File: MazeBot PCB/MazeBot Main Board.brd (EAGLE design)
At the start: 160 x 100 mm, 42 parts, among them IC1 7805TV, IC2 L298, U1 38kHz

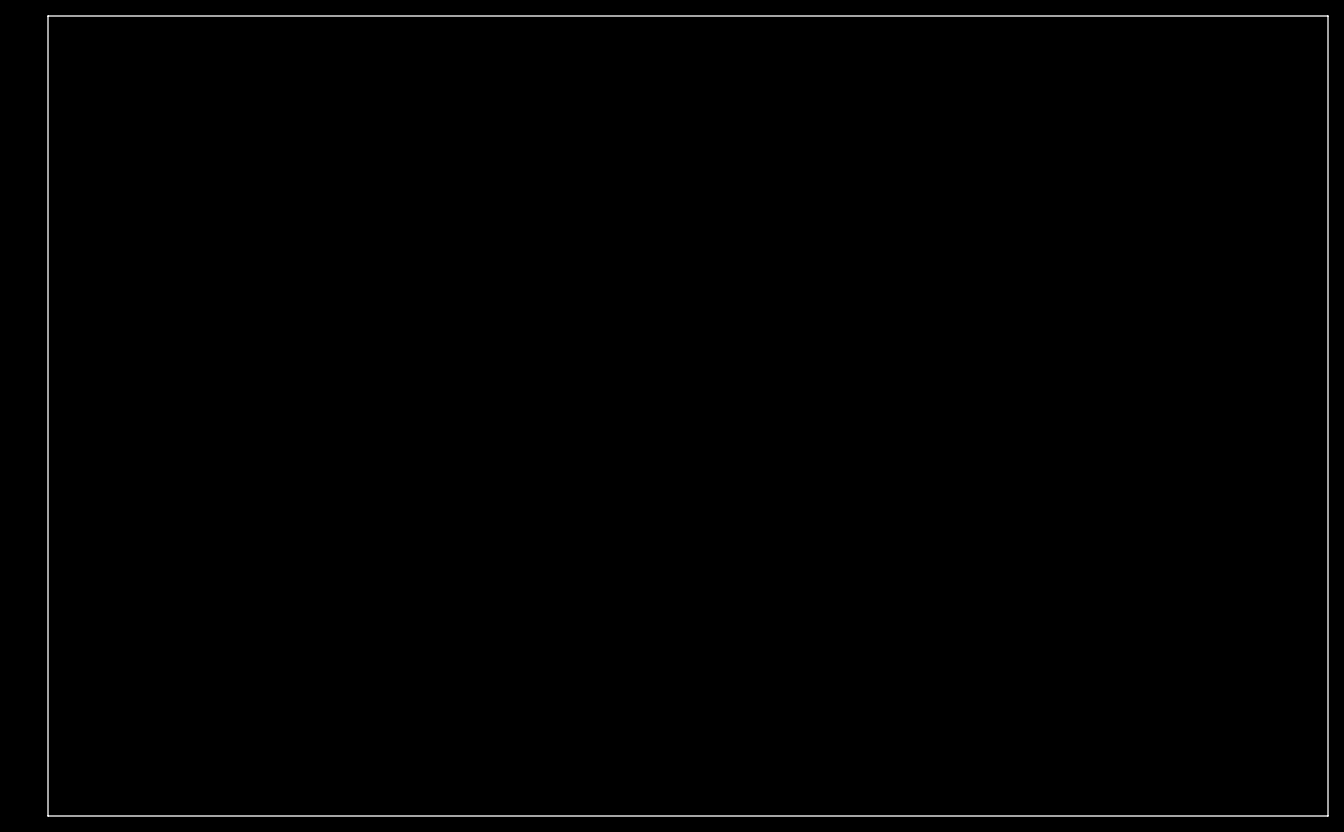
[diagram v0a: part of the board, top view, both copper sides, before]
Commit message: Fix minor shematic issues
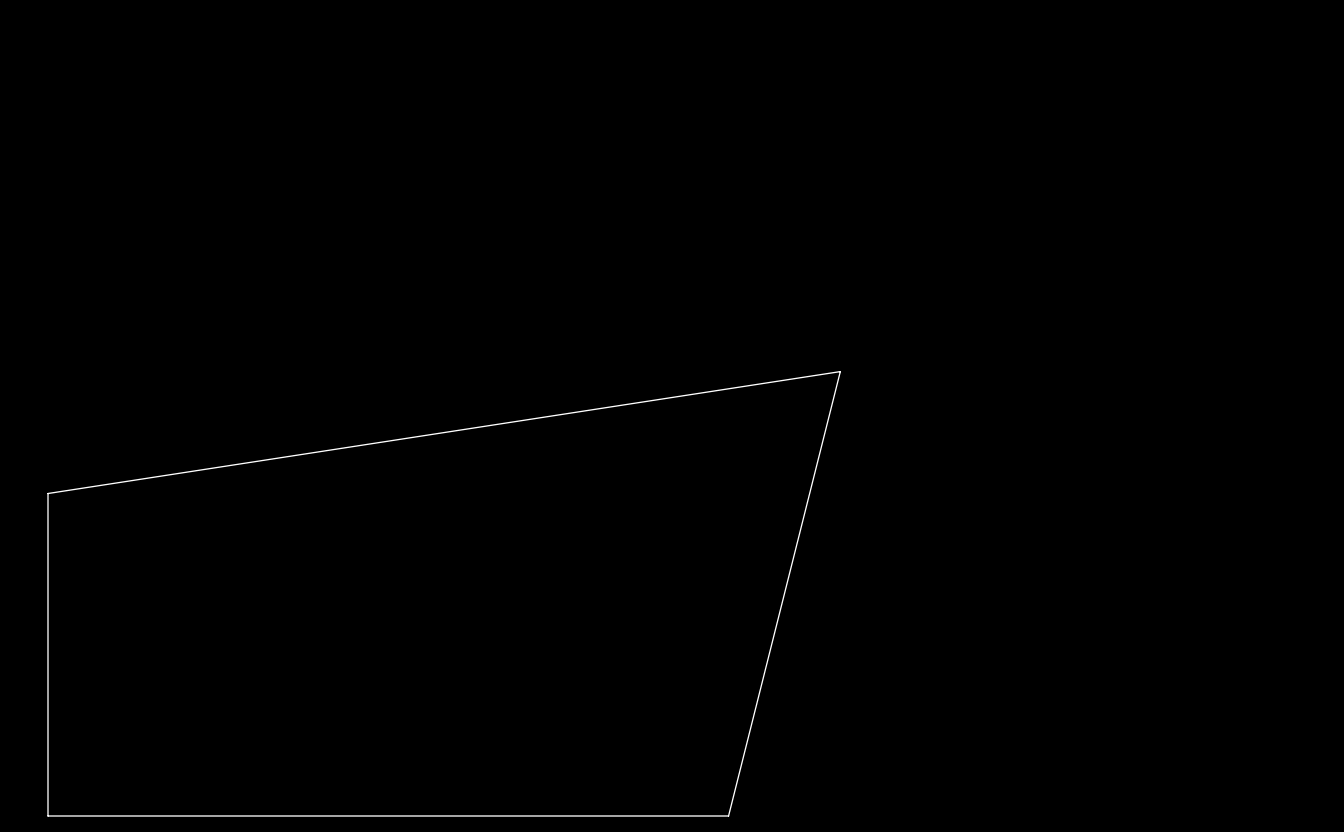
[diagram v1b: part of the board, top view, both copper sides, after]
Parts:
- Q1: value (none) -> 16MHz
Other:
- board size 160 x 100 mm -> 99 x 55.5 mm
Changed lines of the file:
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@@
 <board>
 <plain>
-<wire x1="0" y1="0" x2="160" y2="0" width="0" layer="20"/>
-<wire x1="160" y1="0" x2="160" y2="100" width="0" layer="20"/>
-<wire x1="160" y1="100" x2="0" y2="100" width="0" layer="20"/>
-<wire x1="0" y1="100" x2="0" y2="0" width="0" layer="20"/>
+<wire x1="0" y1="0" x2="85.07" y2="0" width="0" layer="20"/>
+<wire x1="85.07" y1="0" x2="99.04" y2="55.55" width="0" layer="20"/>
+<wire x1="99.04" y1="55.55" x2="0" y2="40.31" width="0" layer="20"/>
+<wire x1="0" y1="40.31" x2="0" y2="0" width="0" layer="20"/>
+<dimension x1="0" y1="100" x2="128.27" y2="100.33" x3="64.08593125" y3="119.237746875" textsize="1.778" layer="1"/>
 </plain>
 <attributes>
@@
 <attribute name="VALUE" x="-19.05" y="20.32" size="1.27" layer="27" rot="R90"/>
 </element>
-<element name="Q1" library="special" library_urn="urn:adsk.eagle:library:367" package="QS" package3d_urn="urn:adsk.eagle:package:26647/2" value="" x="-19.05" y="33.02" smashed="yes">
+<element name="Q1" library="special" library_urn="urn:adsk.eagle:library:367" package="QS" package3d_urn="urn:adsk.eagle:package:26647/2" value="16MHz" x="-19.05" y="33.02" smashed="yes">
 <attribute name="NAME" x="-24.13" y="35.687" size="1.27" layer="25" ratio="10"/>
 <attribute name="VALUE" x="-24.13" y="29.083" size="1.27" layer="27" ratio="10"/>

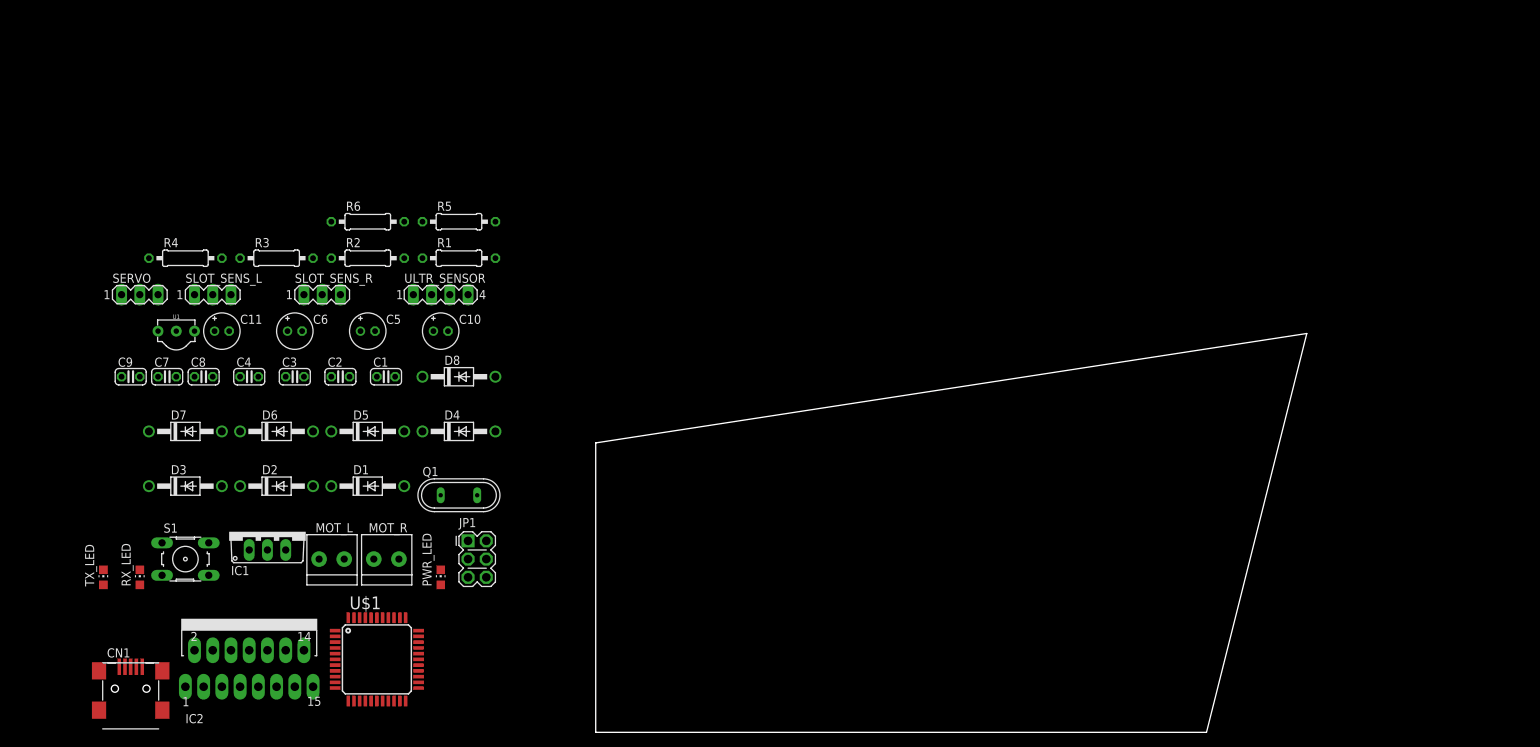
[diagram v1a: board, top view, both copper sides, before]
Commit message: Add power in terminal
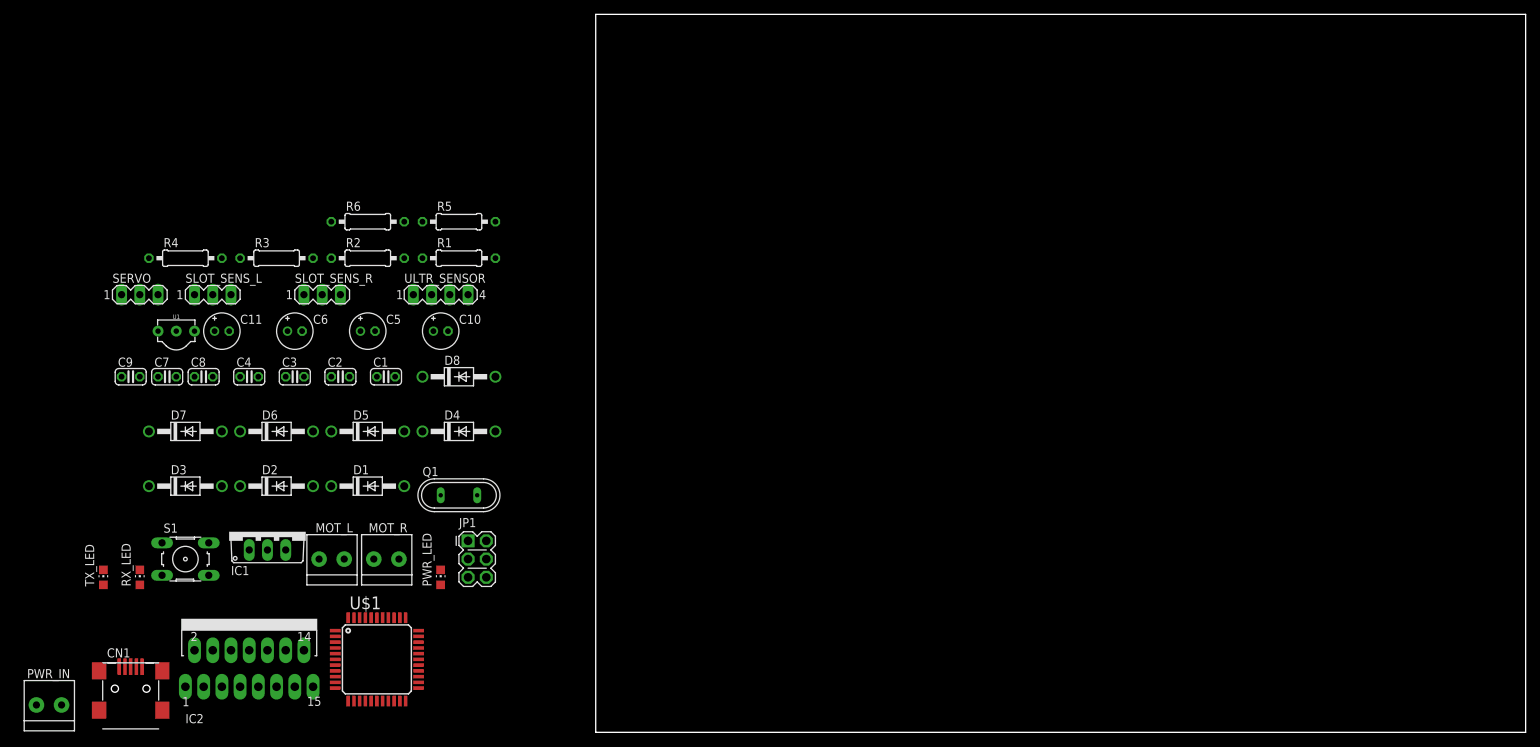
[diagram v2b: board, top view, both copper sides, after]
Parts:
- added PWR_IN: 1X2-3.5MM, adafruit:1X2-3.5MM
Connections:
- net GND: now also PWR_IN.1
- net V+: now also PWR_IN.2
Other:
- board size 99 x 55.5 mm -> 129.5 x 100 mm
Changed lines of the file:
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@@
 <board>
 <plain>
-<wire x1="0" y1="0" x2="85.07" y2="0" width="0" layer="20"/>
-<wire x1="85.07" y1="0" x2="99.04" y2="55.55" width="0" layer="20"/>
-<wire x1="99.04" y1="55.55" x2="0" y2="40.31" width="0" layer="20"/>
-<wire x1="0" y1="40.31" x2="0" y2="0" width="0" layer="20"/>
+<wire x1="0" y1="0" x2="129.52" y2="0" width="0" layer="20"/>
+<wire x1="129.52" y1="0" x2="129.52" y2="100" width="0" layer="20"/>
+<wire x1="129.52" y1="100" x2="0" y2="100" width="0" layer="20"/>
+<wire x1="0" y1="100" x2="0" y2="0" width="0" layer="20"/>
 <dimension x1="0" y1="100" x2="128.27" y2="100.33" x3="64.08593125" y3="119.237746875" textsize="1.778" layer="1"/>
 </plain>
@@
 <attribute name="VALUE" x="-20.955" y="62.611" size="1.27" layer="27" ratio="10"/>
 </element>
+<element name="PWR_IN" library="adafruit" package="1X2-3.5MM" value="1X2-3.5MM" x="-76.2" y="3.81" smashed="yes">
+<attribute name="NAME" x="-73.2" y="8.81" size="1.27" layer="25" rot="R180"/>
+</element>
 </elements>
 <signals>
@@
 <contactref element="D7" pad="C"/>
 <contactref element="D8" pad="C"/>
+<contactref element="PWR_IN" pad="2"/>
+<wire x1="-53.34" y1="11.43" x2="-77.9" y2="3.81" width="0" layer="19" extent="1-1"/>
 <wire x1="-48.26" y1="25.4" x2="-53.34" y2="11.43" width="0" layer="19" extent="1-1"/>
 <wire x1="-49.53" y1="41.91" x2="-48.26" y2="25.4" width="0" layer="19" extent="1-1"/>
@@
 <contactref element="SERVO" pad="3"/>
 <contactref element="C11" pad="-"/>
+<contactref element="PWR_IN" pad="1"/>
+<wire x1="-63.17" y1="9.144" x2="-74.4" y2="3.81" width="0" layer="19" extent="1-1"/>
 <wire x1="-57.15" y1="6.35" x2="-63.17" y2="9.144" width="0" layer="19" extent="1-1"/>
 <wire x1="-48.26" y1="11.43" x2="-57.15" y2="6.35" width="0" layer="19" extent="1-1"/>

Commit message: Route PCB with SMD
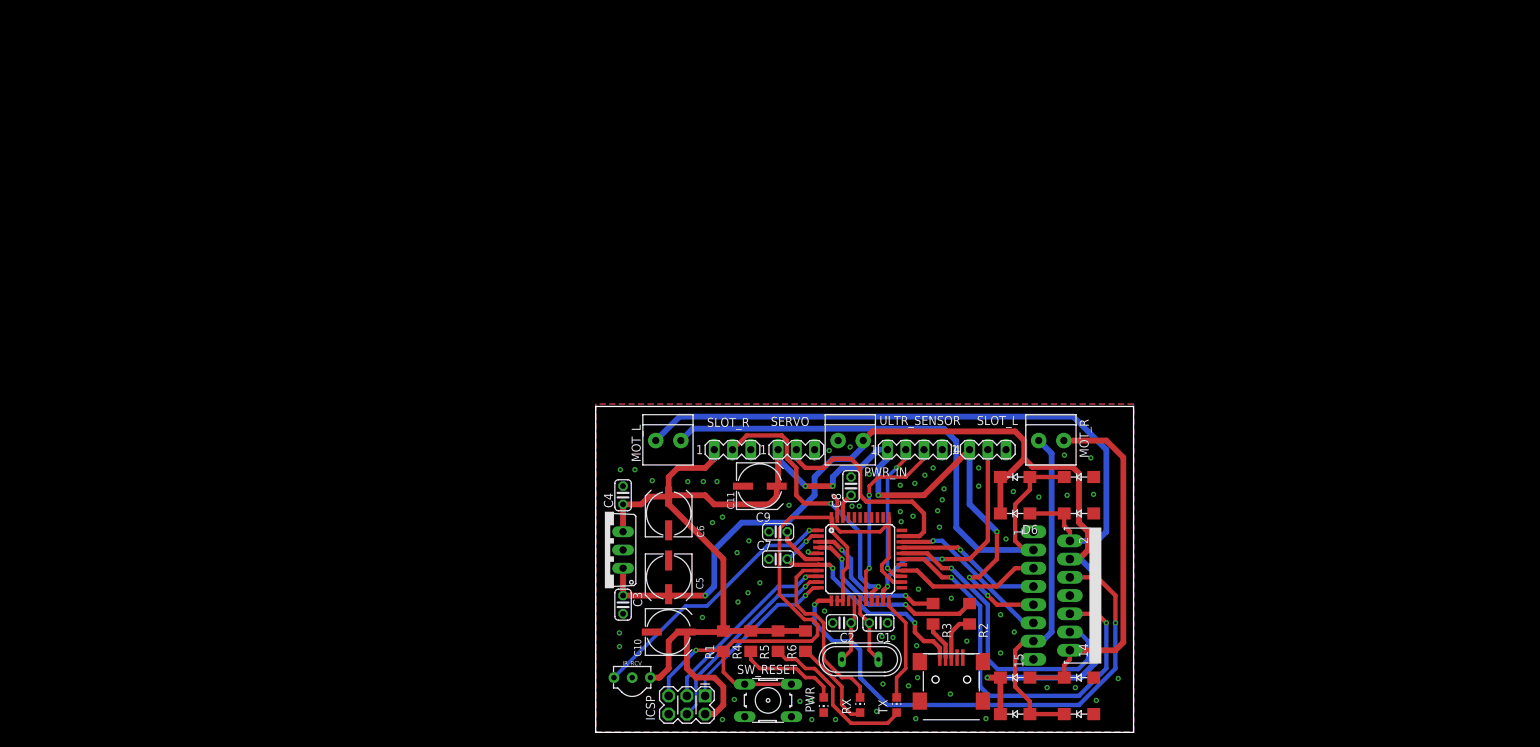
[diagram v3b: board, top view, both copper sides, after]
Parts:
- removed CN1: (no value), adafruit:USB-MINIB
- removed JP1: (no value), arduino_jw:CONN-2X03
- removed PWR_LED, RX_LED, TX_LED: (no value), led:CHIP-LED0805
- removed S1: (no value), switch-omron:B3F-10XX
- removed SLOT_SENS_L, SLOT_SENS_R: (no value), con-lstb:MA03-1
- removed U1: 38kHz, SparkFun-Sensors:TSOP382
- added ICSP: (no value), arduino_jw:CONN-2X03
- added IR_RCV: 38kHz, SparkFun-Sensors:TSOP382
- added PWR, RX, TX: (no value), led:CHIP-LED0805
- added SLOT_L, SLOT_R: (no value), con-lstb:MA03-1
- added SW_RESET: (no value), switch-omron:B3F-10XX
- added USB: (no value), adafruit:USB-MINIB
- C10, C11, C5, C6: device rcl:E2-5 -> rcl:UD-6,3X5,8_NICHICON
- D1, D2, D3, D4, D5, D6, D7, D8: value 1N4004 -> GF1; device diode:DO41-10 -> diode:SMA-DO214AC
- R1, R2, R3, R4, R5, R6: device rcl:0207/10 -> eagle-ltspice:R1206
- moved D3 128.4 mm to (67.3, 2.54), turned to 180 degrees
- moved D7 122.1 mm to (58.4, 2.54), turned to 180 degrees
- moved PWR_IN 117.7 mm to (35.6, 40.6), turned to 180 degrees
- moved IC2 117.0 mm to (68.6, 19.1), turned to 270 degrees
- moved D2 111.8 mm to (67.3, 35.6), turned to 180 degrees
- moved R3 104.0 mm to (47.0, 16.5), turned to 270 degrees
- moved D6 103.5 mm to (58.4, 30.5), turned to 180 degrees
- moved D1 99.1 mm to (67.3, 30.5), turned to 180 degrees
- moved R2 97.4 mm to (52.1, 16.5), turned to 270 degrees
- moved R4 95.1 mm to (21.6, 12.7), turned to 90 degrees
- moved MOT_R 94.2 mm to (63.5, 40.6), turned to 180 degrees
- moved SERVO 94.0 mm to (27.9, 39.4)
- moved D4 92.9 mm to (67.3, 7.62), turned to 180 degrees
- moved C9 92.7 mm to (25.4, 27.9), turned to 180 degrees
- moved C8 91.4 mm to (35.6, 34.3), turned to 90 degrees
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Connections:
- removed net OUT1_L: D1.C, D6.A, IC2.2, MOT_L.1
- removed net OUT1_R: D3.C, D7.A, IC2.13, MOT_R.1
- removed net OUT2_L: D2.C, D5.A, IC2.3, MOT_L.2
- removed net OUT2_R: D4.C, D8.A, IC2.14, MOT_R.2
- new net MOT1_L: D1.K, D6.A, IC2.2, MOT_L.1
- new net MOT1_R: D3.K, D7.A, IC2.13, MOT_R.1
- new net MOT2_L: D2.K, D5.A, IC2.3, MOT_L.2
- new net MOT2_R: D4.K, D8.A, IC2.14, MOT_R.2
- net +5V: now also ICSP.2, IR_RCV.3, SLOT_L.1, SLOT_R.1; no longer JP1.2, SLOT_SENS_L.1, SLOT_SENS_R.1, U1.3
- net GND: now also ICSP.6, IR_RCV.2, PWR.C, SLOT_L.3, SLOT_R.3, SW_RESET.3, SW_RESET.4, USB.GND; no longer CN1.GND, JP1.6, PWR_LED.C, S1.3, S1.4, SLOT_SENS_L.3, SLOT_SENS_R.3, U1.2
- net IR_RCV: now also IR_RCV.1; no longer U1.1
- net MISO: now also ICSP.1; no longer JP1.1
- net MOSI: now also ICSP.4; no longer JP1.4
- net N$3: now also PWR.A; no longer PWR_LED.A
- net N$4: now also USB.D+; no longer CN1.D+
- net N$5: now also USB.D-; no longer CN1.D-
- net N$6: now also TX.A; no longer TX_LED.A
- net N$7: now also RX.A; no longer RX_LED.A
- net RESET: now also ICSP.5, SW_RESET.1, SW_RESET.2; no longer JP1.5, S1.1, S1.2
- net SCK: now also ICSP.3; no longer JP1.3
- net SLOT_SENS_1: now also SLOT_L.2; no longer SLOT_SENS_L.2
- net SLOT_SENS_2: now also SLOT_R.2; no longer SLOT_SENS_R.2
- net SS: now also RX.C; no longer RX_LED.C
- net TX_LED: now also TX.C; no longer TX_LED.C
- net UVCC: now also USB.VBUS; no longer CN1.VBUS
- net V+: now also D5.K, D6.K, D7.K, D8.K; no longer D5.C, D6.C, D7.C, D8.C
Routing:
- net +5V: track 0.00 -> 185.3 mm, vias 0 -> 6
- net V+: track 0.00 -> 149.5 mm, vias 0 -> 2
- net RESET: track 0.00 -> 99.8 mm, vias 0 -> 1
- net MOT1_L: track 0.00 -> 92.0 mm
- net MOT2_L: track 0.00 -> 81.4 mm
- net EN_L: track 0.00 -> 73.7 mm, vias 0 -> 2
- net IN1_R: track 0.00 -> 56.5 mm, vias 0 -> 2
- net MOT2_R: track 0.00 -> 51.3 mm
- net MOT1_R: track 0.00 -> 48.1 mm
- net IN2_R: track 0.00 -> 43.3 mm, vias 0 -> 1
- net SLOT_SENS_2: track 0.00 -> 39.6 mm, vias 0 -> 2
- net IR_RCV: track 0.00 -> 37.0 mm, vias 0 -> 1
- net UVCC: track 0.00 -> 35.0 mm, vias 0 -> 3
- net SLOT_SENS_1: track 0.00 -> 32.3 mm, vias 0 -> 2
- net SERVO: track 0.00 -> 31.4 mm
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- added copper zone on layer 1, net GND
- added copper zone on layer 16, net GND
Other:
- board size 129.5 x 100 mm -> 74.9 x 45.4 mm
